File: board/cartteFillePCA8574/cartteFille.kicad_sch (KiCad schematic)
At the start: 13 parts, among them U1 LM358, U201 PCA8574D,518, U202 PCA8574D,518

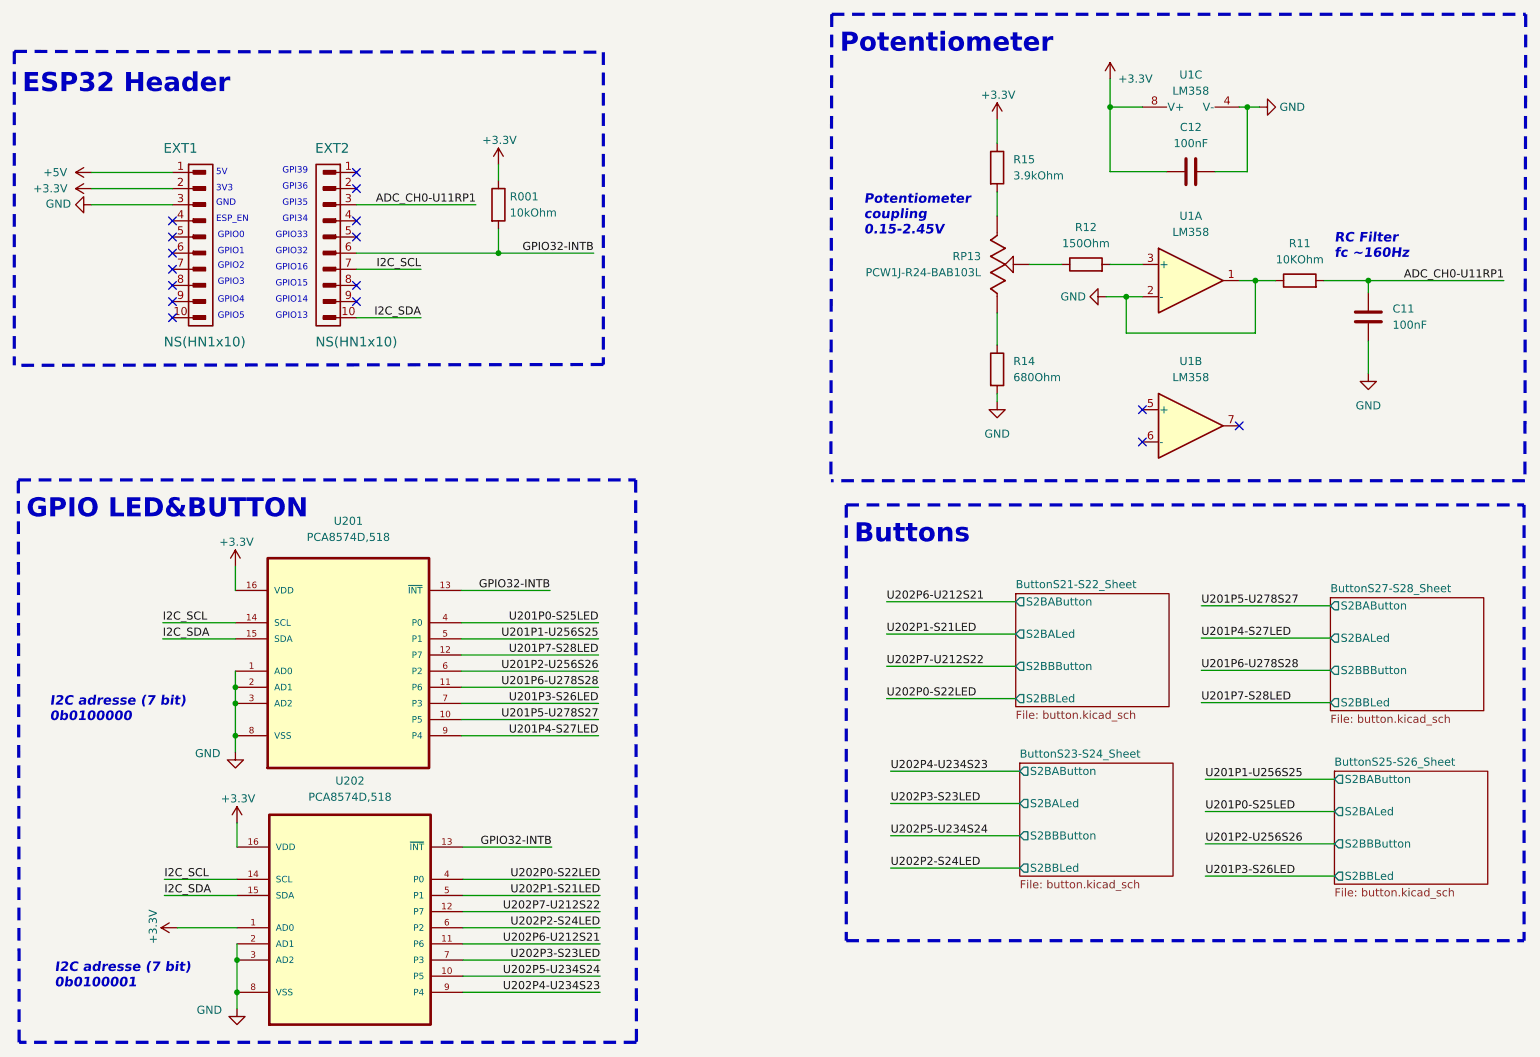
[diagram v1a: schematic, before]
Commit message: commit_V2_PCB
seciond version of pcb final version with gerbert fils
ZIP of the gerber = gerbert_V2
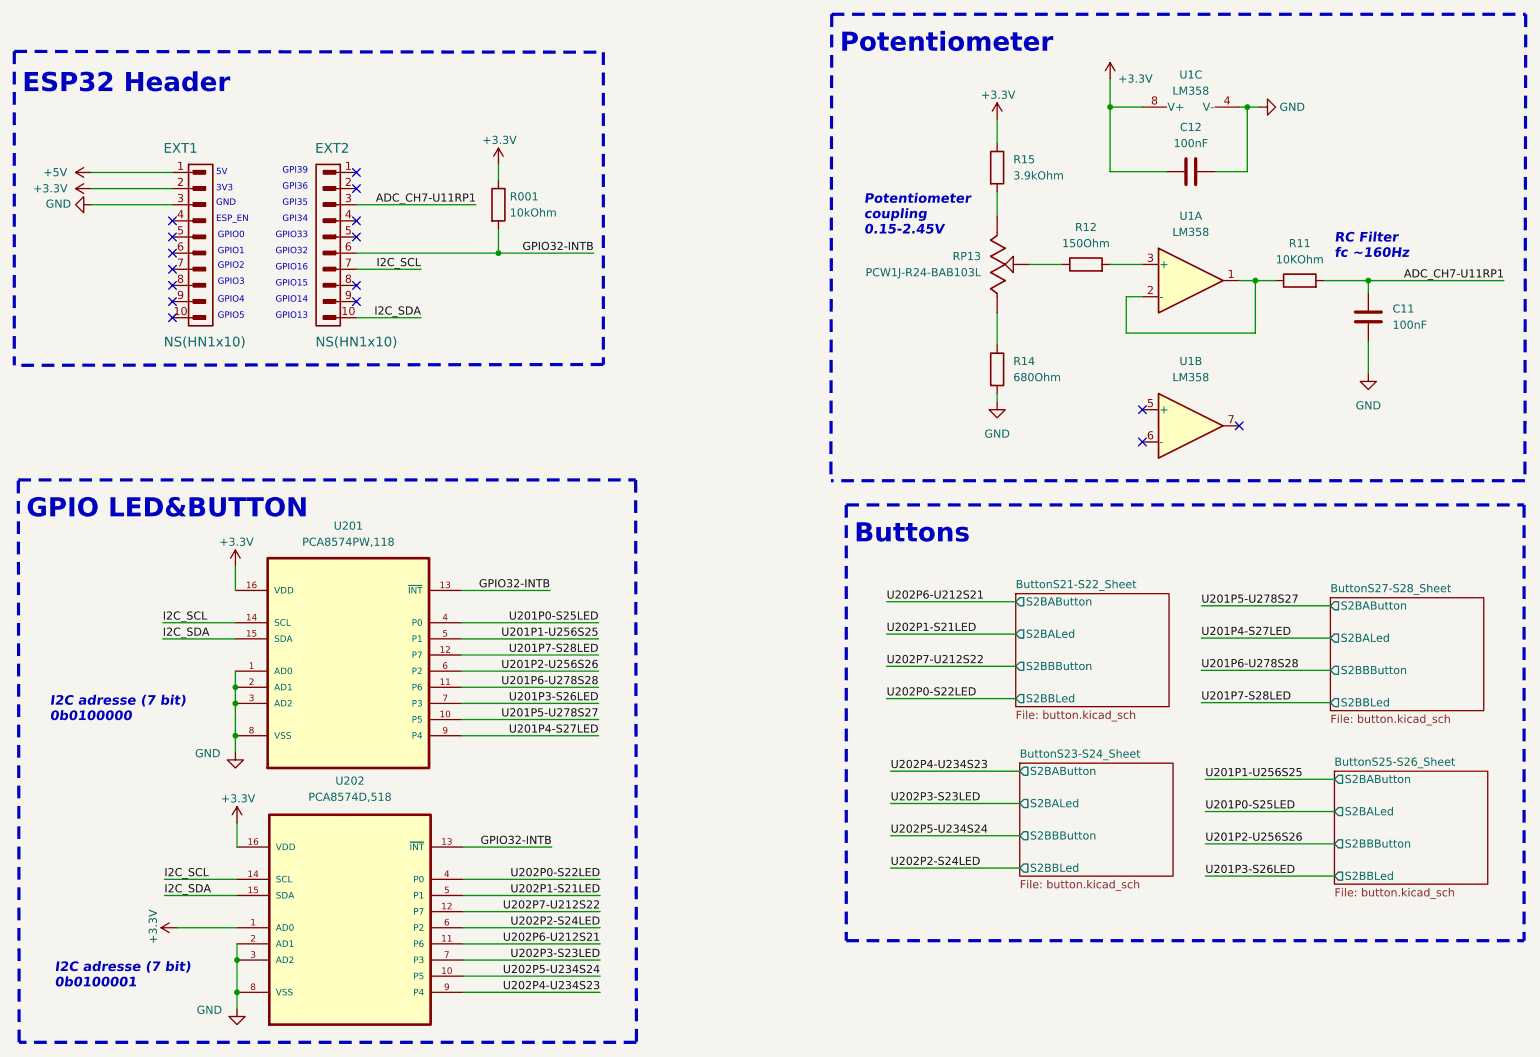
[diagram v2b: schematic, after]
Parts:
- U201: value PCA8574D,518 -> PCA8574PW,118; footprint PCA8574D_518:SOIC127P1032X265-16N -> SOP65P640X110-16N:SOP65P640X110-16N
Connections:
- net GND: no longer R11.1, U1.1, U1.2 (-)
- net ADC_CH0-U11RP1 renamed ADC_CH7-U11RP1
- new net: R11.1, U1.1, U1.2 (-)
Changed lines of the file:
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@@
   (junction (at 205.994 31.877) (diameter 0) (color 0 0 0 0)
-  )
-  (junction (at 208.534 61.722) (diameter 0) (color 0 0 0 0)
   )
   (junction (at 68.326 130.81) (diameter 0) (color 0 0 0 0)
@@
     (stroke (width 0) (type default) (color 0 0 0 0))
   )
-  (wire (pts (xy 205.359 61.722) (xy 208.534 61.722))
-    (stroke (width 0) (type default) (color 0 0 0 0))
-  )
   (wire (pts (xy 103.886 125.73) (xy 125.476 125.73))
     (stroke (width 0) (type default) (color 0 0 0 0))
@@
     (effects (font (size 1.27 1.27)) (justify right bottom))
   )
-  (label "ADC_CH0-U11RP1" (at 267.97 59.182 180)
+  (label "ADC_CH7-U11RP1" (at 267.97 59.182 180)
     (effects (font (size 1.27 1.27)) (justify right bottom))
   )
@@
     (effects (font (size 1.27 1.27)) (justify right bottom))
   )
-  (label "ADC_CH0-U11RP1" (at 106.172 47.244 180)
+  (label "ADC_CH7-U11RP1" (at 106.172 47.244 180)
     (effects (font (size 1.27 1.27)) (justify right bottom))
   )
@@
     (property "Datasheet" "" (id 3) (at 45.72 44.704 0)
       (effects (font (size 1.524 1.524)))
-    )
-    (pin "1")
-  )
-  (symbol (lib_id "power:GND") (at 205.359 61.722 270) (unit 1)
-    (in_bom yes) (on_board yes) (fields_autoplaced)
-    (property "Reference" "#PWR0150" (id 0) (at 199.009 61.722 0)
-      (effects (font (size 1.27 1.27)) hide)
-    )
-    (property "Value" "GND" (id 1) (at 202.184 61.7219 90)
-      (effects (font (size 1.27 1.27)) (justify right))
-    )
-    (property "Footprint" "" (id 2) (at 205.359 61.722 0)
-      (effects (font (size 1.27 1.27)) hide)
-    )
-    (property "Datasheet" "" (id 3) (at 205.359 61.722 0)
-      (effects (font (size 1.27 1.27)) hide)
     )
     (pin "1")
@@
   (symbol (lib_name "PCA8574D,518_1") (lib_id "PCA8574:PCA8574D,518") (at 86.106 115.57 0) (unit 1)
     (in_bom yes) (on_board yes) (fields_autoplaced)
-    (property "Reference" "U201" (id 0) (at 86.106 97.028 0))
-    (property "Value" "PCA8574D,518" (id 1) (at 86.106 99.568 0))
-    (property "Footprint" "PCA8574D_518:SOIC127P1032X265-16N" (id 2) (at 86.106 115.57 0)
+    (property "Reference" "U201" (id 0) (at 86.106 97.79 0))
+    (property "Value" "PCA8574PW,118" (id 1) (at 86.106 100.33 0))
+    (property "Footprint" "SOP65P640X110-16N:SOP65P640X110-16N" (id 2) (at 86.106 115.57 0)
       (effects (font (size 1.27 1.27)) (justify left bottom) hide)
     )
@@
       (reference "#PWR0109") (unit 1) (value "+3.3V") (footprint "")
     )
-    (path "/34faa563-3a6c-45da-a97a-1857ce1dc6ab/cf891bab-7440-4980-a847-91e399f53e4f"
-      (reference "#PWR0110") (unit 1) (value "+5V") (footprint "")
+    (path "/34faa563-3a6c-45da-a97a-1857ce1dc6ab/ecae09b9-3f5b-4de9-b4ca-13626ad4de37"
+      (reference "#PWR0110") (unit 1) (value "+3.3V") (footprint "")
     )
     (path "/34faa563-3a6c-45da-a97a-1857ce1dc6ab/4bde38a4-00f0-46a2-947c-23cbd7bf8162"
@@
       (reference "#PWR0115") (unit 1) (value "GND") (footprint "")
     )
-    (path "/34faa563-3a6c-45da-a97a-1857ce1dc6ab/4aa095a6-7e90-4a68-94d5-5f69129a813d"
-      (reference "#PWR0116") (unit 1) (value "+5V") (footprint "")
+    (path "/34faa563-3a6c-45da-a97a-1857ce1dc6ab/3127e269-87d1-40dd-a113-1194cff0bb16"
+      (reference "#PWR0116") (unit 1) (value "+3.3V") (footprint "")
     )
     (path "/3af5ad0b-084b-47a9-8247-47f815a39c67/9b605348-afe6-494e-b559-3dd09a5ef922"
@@
       (reference "#PWR0124") (unit 1) (value "GND") (footprint "")
     )
-    (path "/3af5ad0b-084b-47a9-8247-47f815a39c67/cf891bab-7440-4980-a847-91e399f53e4f"
-      (reference "#PWR0125") (unit 1) (value "+5V") (footprint "")
+    (path "/e7e1f6df-acb3-430f-8a1c-7326237aadfd/ecae09b9-3f5b-4de9-b4ca-13626ad4de37"
+      (reference "#PWR0125") (unit 1) (value "+3.3V") (footprint "")
     )
     (path "/3af5ad0b-084b-47a9-8247-47f815a39c67/4bde38a4-00f0-46a2-947c-23cbd7bf8162"
@@
       (reference "#PWR0128") (unit 1) (value "+3.3V") (footprint "")
     )
-    (path "/3af5ad0b-084b-47a9-8247-47f815a39c67/4aa095a6-7e90-4a68-94d5-5f69129a813d"
-      (reference "#PWR0129") (unit 1) (value "+5V") (footprint "")
-    )
-    (path "/e7e1f6df-acb3-430f-8a1c-7326237aadfd/cf891bab-7440-4980-a847-91e399f53e4f"
-      (reference "#PWR0130") (unit 1) (value "+5V") (footprint "")
+    (path "/e7e1f6df-acb3-430f-8a1c-7326237aadfd/3127e269-87d1-40dd-a113-1194cff0bb16"
+      (reference "#PWR0129") (unit 1) (value "+3.3V") (footprint "")
+    )
+    (path "/3af5ad0b-084b-47a9-8247-47f815a39c67/ecae09b9-3f5b-4de9-b4ca-13626ad4de37"
+      (reference "#PWR0130") (unit 1) (value "+3.3V") (footprint "")
     )
     (path "/959f0989-468f-4342-bb75-13793619e195"
@@
       (reference "#PWR0142") (unit 1) (value "+3.3V") (footprint "")
     )
-    (path "/282bfcd7-7ad4-40a1-a65a-a67ea836be39/cf891bab-7440-4980-a847-91e399f53e4f"
-      (reference "#PWR0143") (unit 1) (value "+5V") (footprint "")
+    (path "/3af5ad0b-084b-47a9-8247-47f815a39c67/3127e269-87d1-40dd-a113-1194cff0bb16"
+      (reference "#PWR0143") (unit 1) (value "+3.3V") (footprint "")
     )
     (path "/b8f02cda-c715-4a7a-bd9f-965cb033123b"
@@
       (reference "#PWR0149") (unit 1) (value "GND") (footprint "")
     )
-    (path "/48f5724f-61bd-41b7-afae-d250d82f87b8"
-      (reference "#PWR0150") (unit 1) (value "GND") (footprint "")
+    (path "/282bfcd7-7ad4-40a1-a65a-a67ea836be39/ecae09b9-3f5b-4de9-b4ca-13626ad4de37"
+      (reference "#PWR0150") (unit 1) (value "+3.3V") (footprint "")
     )
     (path "/ac1309c4-de4a-4c7e-9b27-983a7a4faa4a"
       (reference "#PWR0151") (unit 1) (value "GND") (footprint "")
     )
-    (path "/e7e1f6df-acb3-430f-8a1c-7326237aadfd/4aa095a6-7e90-4a68-94d5-5f69129a813d"
-      (reference "#PWR0152") (unit 1) (value "+5V") (footprint "")
-    )
-    (path "/282bfcd7-7ad4-40a1-a65a-a67ea836be39/4aa095a6-7e90-4a68-94d5-5f69129a813d"
-      (reference "#PWR0153") (unit 1) (value "+5V") (footprint "")
+    (path "/282bfcd7-7ad4-40a1-a65a-a67ea836be39/3127e269-87d1-40dd-a113-1194cff0bb16"
+      (reference "#PWR0152") (unit 1) (value "+3.3V") (footprint "")
     )
     (path "/cc71f50e-855c-40e9-beb2-ae15adf374ba"
@@
     )
     (path "/34faa563-3a6c-45da-a97a-1857ce1dc6ab/591fbeb8-c3a4-49de-ae4d-8c961304b310"
-      (reference "R213") (unit 1) (value "150Ohm") (footprint "Resistor_SMD:R_0603_1608Metric")
+      (reference "R213") (unit 1) (value "68Ohm") (footprint "Resistor_SMD:R_0603_1608Metric")
     )
     (path "/34faa563-3a6c-45da-a97a-1857ce1dc6ab/48abcbca-0b7c-4b07-9783-2f0b28557d84"
@@
     )
     (path "/34faa563-3a6c-45da-a97a-1857ce1dc6ab/3ed80a9b-b613-4878-afce-e244385fa149"
-      (reference "R223") (unit 1) (value "150Ohm") (footprint "Resistor_SMD:R_0603_1608Metric")
+      (reference "R223") (unit 1) (value "68Ohm") (footprint "Resistor_SMD:R_0603_1608Metric")
     )
     (path "/e7e1f6df-acb3-430f-8a1c-7326237aadfd/512ccdc1-4692-4d1a-90ac-f3d93f19ae32"
@@
     )
     (path "/e7e1f6df-acb3-430f-8a1c-7326237aadfd/591fbeb8-c3a4-49de-ae4d-8c961304b310"
-      (reference "R233") (unit 1) (value "150Ohm") (footprint "Resistor_SMD:R_0603_1608Metric")
+      (reference "R233") (unit 1) (value "68Ohm") (footprint "Resistor_SMD:R_0603_1608Metric")
     )
     (path "/e7e1f6df-acb3-430f-8a1c-7326237aadfd/48abcbca-0b7c-4b07-9783-2f0b28557d84"
@@
     )
     (path "/e7e1f6df-acb3-430f-8a1c-7326237aadfd/3ed80a9b-b613-4878-afce-e244385fa149"
-      (reference "R243") (unit 1) (value "150Ohm") (footprint "Resistor_SMD:R_0603_1608Metric")
+      (reference "R243") (unit 1) (value "68Ohm") (footprint "Resistor_SMD:R_0603_1608Metric")
     )
     (path "/3af5ad0b-084b-47a9-8247-47f815a39c67/512ccdc1-4692-4d1a-90ac-f3d93f19ae32"
@@
     )
     (path "/3af5ad0b-084b-47a9-8247-47f815a39c67/591fbeb8-c3a4-49de-ae4d-8c961304b310"
-      (reference "R253") (unit 1) (value "150Ohm") (footprint "Resistor_SMD:R_0603_1608Metric")
+      (reference "R253") (unit 1) (value "68Ohm") (footprint "Resistor_SMD:R_0603_1608Metric")
     )
     (path "/3af5ad0b-084b-47a9-8247-47f815a39c67/48abcbca-0b7c-4b07-9783-2f0b28557d84"
@@
     )
     (path "/3af5ad0b-084b-47a9-8247-47f815a39c67/3ed80a9b-b613-4878-afce-e244385fa149"
-      (reference "R263") (unit 1) (value "150Ohm") (footprint "Resistor_SMD:R_0603_1608Metric")
+      (reference "R263") (unit 1) (value "68Ohm") (footprint "Resistor_SMD:R_0603_1608Metric")
     )
     (path "/282bfcd7-7ad4-40a1-a65a-a67ea836be39/512ccdc1-4692-4d1a-90ac-f3d93f19ae32"
@@
     )
     (path "/282bfcd7-7ad4-40a1-a65a-a67ea836be39/591fbeb8-c3a4-49de-ae4d-8c961304b310"
-      (reference "R273") (unit 1) (value "150Ohm") (footprint "Resistor_SMD:R_0603_1608Metric")
+      (reference "R273") (unit 1) (value "68Ohm") (footprint "Resistor_SMD:R_0603_1608Metric")
     )
     (path "/282bfcd7-7ad4-40a1-a65a-a67ea836be39/48abcbca-0b7c-4b07-9783-2f0b28557d84"
@@
     )
     (path "/282bfcd7-7ad4-40a1-a65a-a67ea836be39/3ed80a9b-b613-4878-afce-e244385fa149"
-      (reference "R283") (unit 1) (value "150Ohm") (footprint "Resistor_SMD:R_0603_1608Metric")
+      (reference "R283") (unit 1) (value "68Ohm") (footprint "Resistor_SMD:R_0603_1608Metric")
     )
     (path "/b823fe53-23aa-4ee7-a030-5fce0a43fad8"
@@
     )
     (path "/f6bf9502-3541-4ac2-a411-4155f1ab5df0"
-      (reference "U201") (unit 1) (value "PCA8574D,518") (footprint "PCA8574D_518:SOIC127P1032X265-16N")
+      (reference "U201") (unit 1) (value "PCA8574PW,118") (footprint "SOP65P640X110-16N:SOP65P640X110-16N")
     )
     (path "/e7980008-fd9d-4187-8e1c-798ba7022c89"
